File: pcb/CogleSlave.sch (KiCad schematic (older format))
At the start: 7 parts, among them P1 CONN_01X04, P2 CONN_01X04, P3 CONN_01X08, U1 PCF8591T

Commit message: 基板レイアウトを修正 1.2
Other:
- moved on the sheet: C1, P1, P2, P3, R1, R2, U1

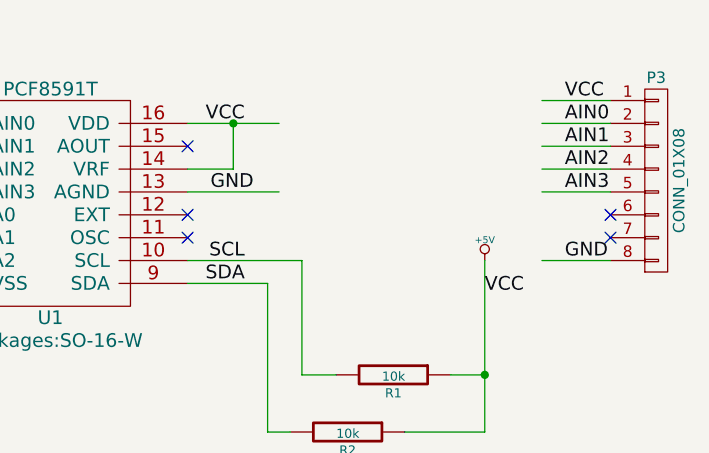
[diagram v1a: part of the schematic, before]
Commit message: Arduino向けライブラリv1.0を追加
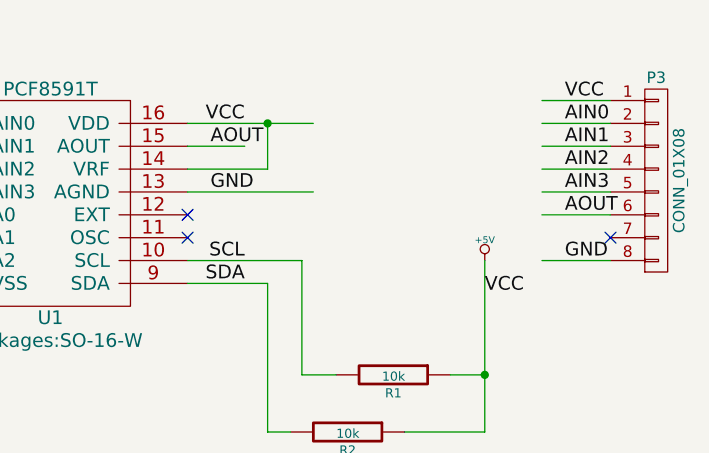
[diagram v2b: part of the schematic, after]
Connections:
- net labels added: AOUT
- wire segments 40 -> 42
- no-connect marks 6 -> 4
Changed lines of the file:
@@
 	4950 4150 4700 4150
 Wire Wire Line
-	6150 3450 6550 3450
+	6150 3450 6700 3450
 Text Label 6400 3450 2    60   ~ 0
 VCC
@@
 VCC
 Wire Wire Line
-	6150 3650 6350 3650
+	6150 3650 6500 3650
 Wire Wire Line
-	6350 3650 6350 3450
-Connection ~ 6350 3450
+	6500 3650 6500 3450
+Connection ~ 6500 3450
 Wire Wire Line
-	6150 3750 6550 3750
+	6150 3750 6700 3750
 Text Label 6250 3750 0    60   ~ 0
 GND
@@
 NoConn ~ 6150 3850
 NoConn ~ 6150 3950
-NoConn ~ 8000 3850
 NoConn ~ 8000 3950
 Wire Wire Line
@@
 Text Label 4100 4050 0    60   ~ 0
 A2
-NoConn ~ 6150 3550
 Text Label 4750 4150 0    60   ~ 0
 GND
@@
 Wire Wire Line
 	6500 4800 6600 4800
+Wire Wire Line
+	6150 3550 6400 3550
+Text Label 6250 3550 0    60   ~ 0
+AOUT
+Wire Wire Line
+	8000 3850 7700 3850
+Text Label 7800 3850 0    60   ~ 0
+AOUT
 $EndSCHEMATC
